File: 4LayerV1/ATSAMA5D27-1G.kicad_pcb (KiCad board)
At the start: 4 copper layers, 22.9 x 50.8 mm, 172 parts, among them J1 Conn_01x16, J2 Conn_01x12, J3 USB_B_Micro, J4 Conn_01x02, J5 Conn_01x02, J6 1051620001, J7 USB_B_Micro, Q1 BSS138, Q2 BSS138, Q3 BSS138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

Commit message: Create local footprint library and copy over custom footprints.
In theory you should be able to update the PCB from the Schematic now
with no changes, however, there seems to be an issue with the USB
port PCB layout not matching the schematic - perhaps due to the swap
from a USB B to a USB A component?
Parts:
- J3: footprint OSD3358-CHIP:USB_Micro-B_Molex-105017-0001 -> ATSAMA5D27-1G:USB_Micro-B_Molex-105017-0001
- J6: footprint footprints:1051620001 -> ATSAMA5D27-1G:1051620001
- J7: footprint 10104111-0001LF:FRAMATOME_10104111-0001LF -> ATSAMA5D27-1G:FRAMATOME_10104111-0001LF
- L11, L12, L6: footprint footprints:L_0603 -> ATSAMA5D27-1G:L_0603
- NT1, NT2: footprint footprints:NetTie-2_SMD_Padsmall -> ATSAMA5D27-1G:NetTie-2_SMD_Padsmall
- PB1: footprint OSD3358-CHIP:MINI_PUSHBUTTON -> ATSAMA5D27-1G:MINI_PUSHBUTTON
- U1: footprint ATSAMA5D27C-D1G-CU:BGA289C80P17X17_1400X1400X120N -> ATSAMA5D27-1G:BGA289C80P17X17_1400X1400X120N
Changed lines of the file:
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@@
     (add_net nPBSTAT)
   )
-  (module footprints:1051620001 (layer B.Cu)
+  (module ATSAMA5D27-1G:1051620001 (layer B.Cu)
     (at 135.03726 116.64162 180)
     (descr 1051620001)
@@
     )
   )
-  (module footprints:NetTie-2_SMD_Padsmall (layer F.Cu)
+  (module ATSAMA5D27-1G:NetTie-2_SMD_Padsmall (layer F.Cu)
     (at 135.38726 101.08962)
     (descr "Net tie, 2 pin, 0.5mm square SMD pads")
@@
     )
   )
-  (module footprints:L_0603 (layer B.Cu)
+  (module ATSAMA5D27-1G:L_0603 (layer B.Cu)
     (at 142.2097 92.334451 270)
     (descr "Resistor SMD 0603, reflow soldering, Vishay (see dcrcw.pdf)")
@@
     )
   )
-  (module footprints:L_0603 (layer B.Cu)
+  (module ATSAMA5D27-1G:L_0603 (layer B.Cu)
     (at 140.39096 92.38942 270)
     (descr "Resistor SMD 0603, reflow soldering, Vishay (see dcrcw.pdf)")
@@
     )
   )
-  (module footprints:L_0603 (layer B.Cu)
+  (module ATSAMA5D27-1G:L_0603 (layer B.Cu)
     (at 141.74986 100.53082 270)
     (descr "Resistor SMD 0603, reflow soldering, Vishay (see dcrcw.pdf)")
@@
     )
   )
-  (module ATSAMA5D27C-D1G-CU:BGA289C80P17X17_1400X1400X120N (layer F.Cu)
+  (module ATSAMA5D27-1G:BGA289C80P17X17_1400X1400X120N (layer F.Cu)
     (at 135.12452 103.08938 180)
     (attr smd)
@@
     )
   )
-  (module OSD3358-CHIP:USB_Micro-B_Molex-105017-0001 (layer F.Cu)
+  (module ATSAMA5D27-1G:USB_Micro-B_Molex-105017-0001 (layer F.Cu)
     (at 135.12452 71.97438 180)
     (descr http://www.molex.com/pdm_docs/sd/1050170001_sd.pdf)
@@
     )
   )
-  (module OSD3358-CHIP:MINI_PUSHBUTTON (layer F.Cu)
+  (module ATSAMA5D27-1G:MINI_PUSHBUTTON (layer F.Cu)
     (at 139.66198 117.4777 180)
     (attr smd)
@@
     )
   )
-  (module 10104111-0001LF:FRAMATOME_10104111-0001LF (layer B.Cu)
+  (module ATSAMA5D27-1G:FRAMATOME_10104111-0001LF (layer B.Cu)
     (at 144.44226 80.16002 270)
     (attr smd)
@@
     )
   )
-  (module footprints:NetTie-2_SMD_Padsmall (layer B.Cu)
+  (module ATSAMA5D27-1G:NetTie-2_SMD_Padsmall (layer B.Cu)
     (at 138.89236 95.48892 90)
     (descr "Net tie, 2 pin, 0.5mm square SMD pads")

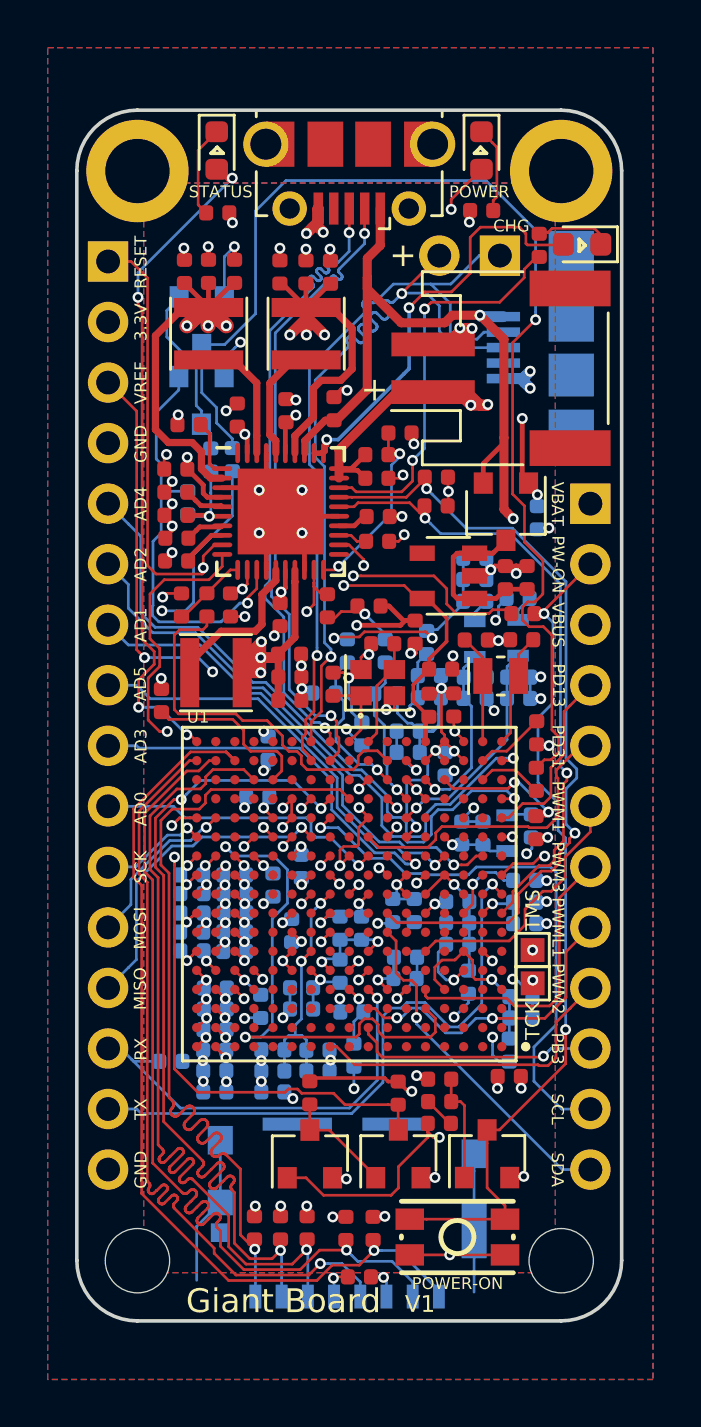
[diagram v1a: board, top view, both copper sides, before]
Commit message: Squeezing in a 0R on the USB A power pin.
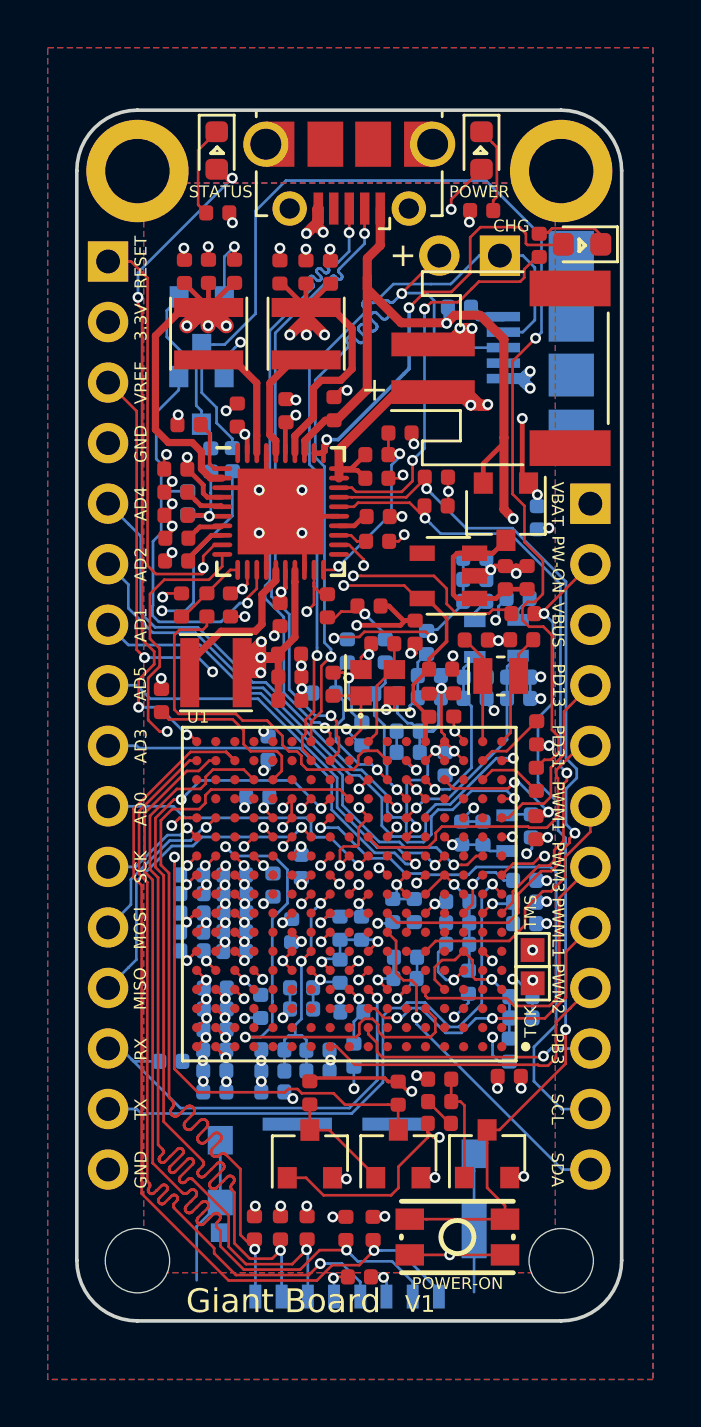
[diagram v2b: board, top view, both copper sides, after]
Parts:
- added R13: 0R, Resistor_SMD:R_0402_1005Metric, B.Cu at (139.7, 78.5)
- J7: value USB_B_Micro -> USB_AB_Micro
- renumbered TCK to TP1, TMS to TP2
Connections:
- net USBA_M renamed USBA_N
- net USBB_M renamed USBB_N
- J3 pad 4: Net-(J3-Pad4) -> (no net)
- J6 pad 9: Net-(J6-Pad9) -> (no net)
- J7 pad 1: VBUS -> Net-(J7-Pad1)
- J7 pad 4: Net-(J7-Pad4) -> (no net)
- U1 pad A1: Net-(U1-PadA1) -> (no net)
- U1 pad A11: Net-(U1-PadA11) -> (no net)
- U1 pad A2: Net-(U1-PadA2) -> (no net)
- U1 pad A3: Net-(U1-PadA3) -> (no net)
- U1 pad A4: Net-(U1-PadA4) -> (no net)
- U1 pad A5: Net-(U1-PadA5) -> (no net)
- U1 pad A6: Net-(U1-PadA6) -> (no net)
- U1 pad A7: Net-(U1-PadA7) -> (no net)
- U1 pad A8: Net-(U1-PadA8) -> (no net)
- U1 pad A9: Net-(U1-PadA9) -> (no net)
- U1 pad B1: Net-(U1-PadB1) -> (no net)
- U1 pad B10: Net-(U1-PadB10) -> (no net)
- U1 pad B2: Net-(U1-PadB2) -> (no net)
- U1 pad B3: Net-(U1-PadB3) -> (no net)
- U1 pad B4: Net-(U1-PadB4) -> (no net)
- U1 pad B5: Net-(U1-PadB5) -> (no net)
- U1 pad B6: Net-(U1-PadB6) -> (no net)
- U1 pad B7: Net-(U1-PadB7) -> (no net)
- U1 pad B9: Net-(U1-PadB9) -> (no net)
- U1 pad C1: Net-(U1-PadC1) -> (no net)
- U1 pad C2: Net-(U1-PadC2) -> (no net)
- U1 pad C3: Net-(U1-PadC3) -> (no net)
- U1 pad C4: Net-(U1-PadC4) -> (no net)
- U1 pad C6: Net-(U1-PadC6) -> (no net)
- U1 pad C7: Net-(U1-PadC7) -> (no net)
- U1 pad C9: Net-(U1-PadC9) -> (no net)
- U1 pad D1: Net-(U1-PadD1) -> (no net)
- U1 pad D2: Net-(U1-PadD2) -> (no net)
- U1 pad D3: Net-(U1-PadD3) -> (no net)
- U1 pad E1: Net-(U1-PadE1) -> (no net)
- U1 pad E2: Net-(U1-PadE2) -> (no net)
- U1 pad E4: Net-(U1-PadE4) -> (no net)
- U1 pad E5: Net-(U1-PadE5) -> (no net)
- U1 pad E6: Net-(U1-PadE6) -> (no net)
- U1 pad E7: Net-(U1-PadE7) -> (no net)
- U1 pad F1: Net-(U1-PadF1) -> (no net)
- U1 pad F4: Net-(U1-PadF4) -> (no net)
- U1 pad F6: Net-(U1-PadF6) -> (no net)
- U1 pad F7: Net-(U1-PadF7) -> (no net)
- U1 pad G1: Net-(U1-PadG1) -> (no net)
- U1 pad G2: Net-(U1-PadG2) -> (no net)
- U1 pad G3: Net-(U1-PadG3) -> (no net)
- U1 pad G4: Net-(U1-PadG4) -> (no net)
- U1 pad G5: Net-(U1-PadG5) -> (no net)
- U1 pad G6: Net-(U1-PadG6) -> (no net)
- U1 pad G8: Net-(U1-PadG8) -> (no net)
- U1 pad G9: Net-(U1-PadG9) -> (no net)
- U1 pad H4: Net-(U1-PadH4) -> (no net)
- U1 pad H6: Net-(U1-PadH6) -> (no net)
- U1 pad H8: Net-(U1-PadH8) -> (no net)
- U1 pad H9: Net-(U1-PadH9) -> (no net)
- U1 pad J2: Net-(U1-PadJ2) -> (no net)
- U1 pad J3: Net-(U1-PadJ3) -> (no net)
- U1 pad J4: Net-(U1-PadJ4) -> (no net)
- U1 pad J7: Net-(U1-PadJ7) -> (no net)
- U1 pad K2: Net-(U1-PadK2) -> (no net)
- U1 pad K3: Net-(U1-PadK3) -> (no net)
- U1 pad K8: Net-(U1-PadK8) -> (no net)
- U1 pad K9: Net-(U1-PadK9) -> (no net)
- U1 pad L1: Net-(U1-PadL1) -> (no net)
- U1 pad L11: Net-(U1-PadL11) -> (no net)
- U1 pad L3: Net-(U1-PadL3) -> (no net)
- U1 pad L5: Net-(U1-PadL5) -> (no net)
- U1 pad L7: Net-(U1-PadL7) -> (no net)
- U1 pad M10: Net-(U1-PadM10) -> (no net)
- U1 pad M15: Net-(U1-PadM15) -> (no net)
- U1 pad M16: Net-(U1-PadM16) -> (no net)
- U1 pad M2: Net-(U1-PadM2) -> (no net)
- U1 pad M3: PIOBU1 -> (no net)
- U1 pad M5: PIOBU5 -> (no net)
- U1 pad M9: Net-(U1-PadM9) -> (no net)
- U1 pad N11: Net-(U1-PadN11) -> (no net)
- U1 pad N14: Net-(U1-PadN14) -> (no net)
- U1 pad N15: Net-(U1-PadN15) -> (no net)
- U1 pad N2: RXD -> (no net)
- U1 pad N3: PIOBU7 -> (no net)
- U1 pad N4: PIOBU4 -> (no net)
- U1 pad N5: PIOBU6 -> (no net)
- U1 pad N7: Net-(U1-PadN7) -> (no net)
- U1 pad N9: Net-(U1-PadN9) -> (no net)
- U1 pad P13: PWML0 -> (no net)
- U1 pad P14: Net-(U1-PadP14) -> (no net)
- U1 pad P15: Net-(U1-PadP15) -> (no net)
- U1 pad P16: Net-(U1-PadP16) -> (no net)
- U1 pad P17: Net-(U1-PadP17) -> (no net)
- U1 pad P2: PIOBU2 -> (no net)
- U1 pad P3: LOWQ# -> (no net)
- U1 pad P4: PIOBU3 -> (no net)
- U1 pad P8: Net-(U1-PadP8) -> (no net)
- U1 pad R1: Net-(U1-PadR1) -> (no net)
- U1 pad R10: Net-(U1-PadR10) -> (no net)
- U1 pad R11: Net-(U1-PadR11) -> (no net)
- U1 pad R15: Net-(U1-PadR15) -> (no net)
- U1 pad R16: Net-(U1-PadR16) -> (no net)
- U1 pad R17: Net-(U1-PadR17) -> (no net)
- U1 pad R3: Net-(U1-PadR3) -> (no net)
- U1 pad R9: Net-(U1-PadR9) -> (no net)
- U1 pad T12: DATA -> (no net)
- U1 pad T13: Net-(U1-PadT13) -> (no net)
- U1 pad T14: Net-(U1-PadT14) -> (no net)
- U1 pad T8: CLK_AUDIO -> (no net)
- U1 pad U12: STROBE -> (no net)
- U1 pad U13: Net-(U1-PadU13) -> (no net)
- U1 pad U14: Net-(U1-PadU14) -> (no net)
- U1 pad U15: Net-(U1-PadU15) -> (no net)
- U1 pad U16: Net-(U1-PadU16) -> (no net)
- U1 pad U6: Net-(U1-PadU6) -> (no net)
- U1 pad U7: Net-(U1-PadU7) -> (no net)
- U2 pad 21: Net-(U2-Pad21) -> (no net)
- U3 pad 4: Net-(U3-Pad4) -> (no net)
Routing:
- net Net-(J7-Pad1): track 0.00 -> 1.46 mm
- net USBB_N: track 32.2 -> 32.8 mm
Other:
- board text added: "TCK"
- board text added: "TMS"
